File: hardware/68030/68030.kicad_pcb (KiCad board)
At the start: 2 copper layers, 99.1 x 99.1 mm, 20 parts, among them J1 nuMezzanine_4x34, U1 MC68030RC25B

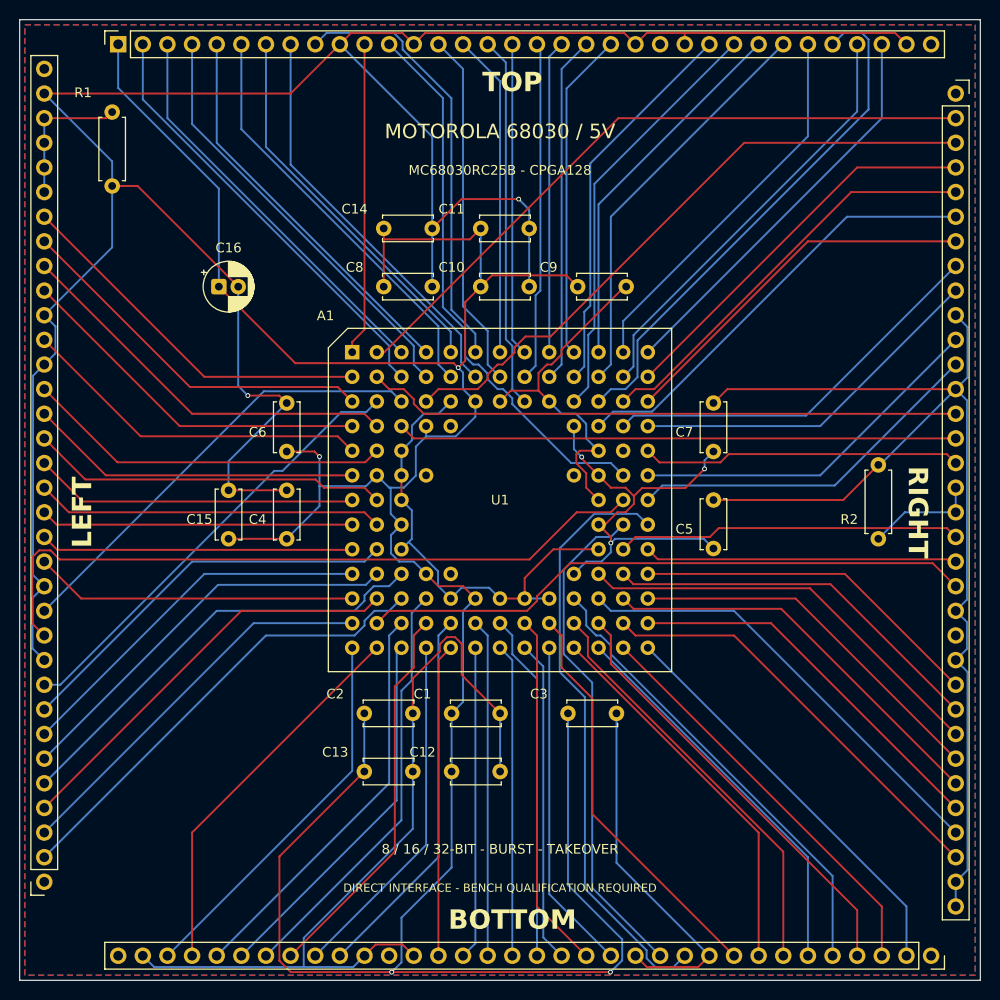
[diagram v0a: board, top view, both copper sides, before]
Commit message: Update mainboard to revision 2
Add an additional 8 bidirectional channels
Replace SPI PSRAM with hyperram
Remove LEDs
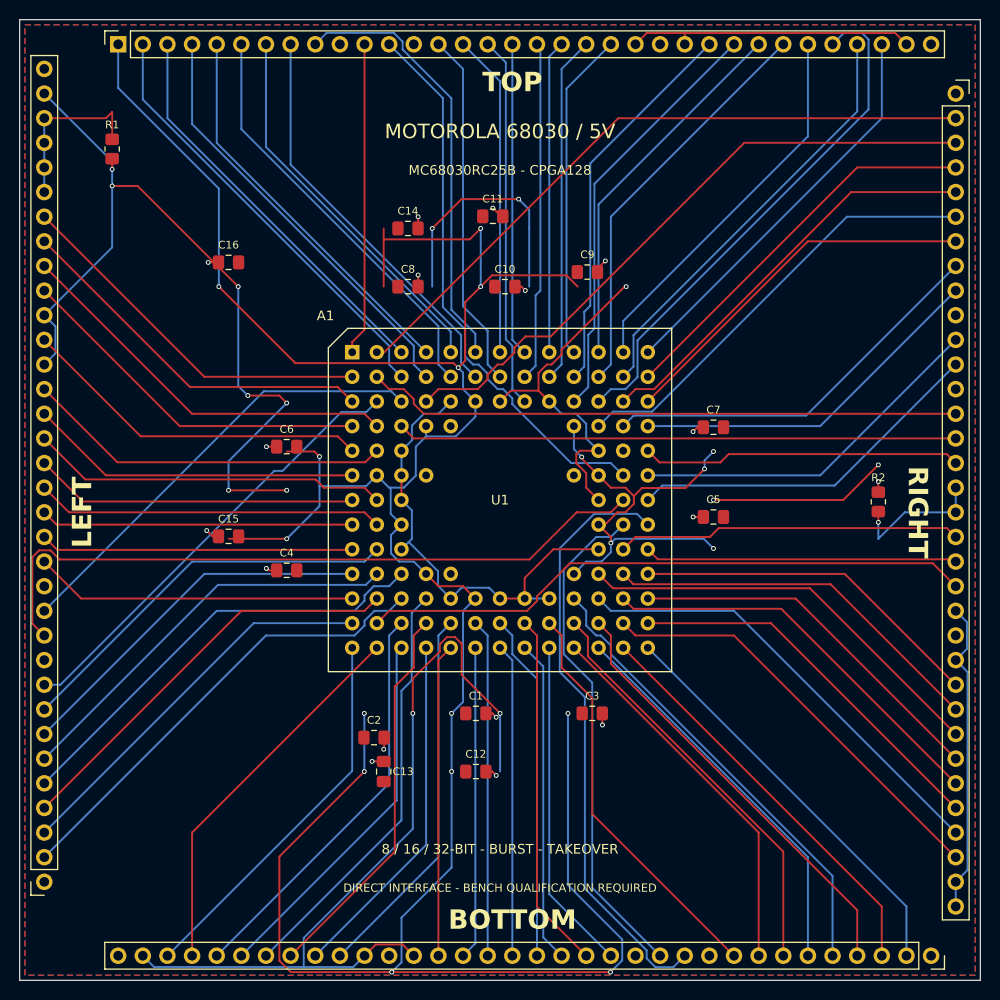
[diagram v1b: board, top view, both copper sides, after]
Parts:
- C1, C10, C11, C12, C13, C14, C15, C2, C3, C4, C5, C6, C7, C8, C9: footprint Capacitor_THT:C_Disc_D5.0mm_W2.5mm_P5.00mm -> Capacitor_SMD:C_0805_2012Metric_Pad1.18x1.45mm_HandSolder
- C16: footprint Capacitor_THT:CP_Radial_D5.0mm_P2.00mm -> Capacitor_SMD:C_0805_2012Metric_Pad1.18x1.45mm_HandSolder
- R1, R2: footprint Resistor_THT:R_Axial_DIN0207_L6.3mm_D2.5mm_P7.62mm_Horizontal -> Resistor_SMD:R_0805_2012Metric_Pad1.20x1.40mm_HandSolder
- moved R1 3.81 mm to (111.0, 59.8)
- moved R2 3.81 mm to (190.0, 96.2)
- moved C4 3.25 mm to (129.0, 103.2), turned to 180 degrees
- moved C5 3.25 mm to (173.0, 97.8), turned to 180 degrees
- moved C16 2.69 mm to (123.0, 71.5), turned to 180 degrees
- moved C2 2.69 mm to (138.0, 120.5)
- moved C1 2.50 mm to (148.5, 118.0)
- moved C10 2.50 mm to (151.5, 74.0)
- moved C12 2.50 mm to (148.5, 124.0)
- moved C14 2.50 mm to (141.5, 68.0)
- moved C3 2.50 mm to (160.5, 118.0)
- moved C7 2.50 mm to (173.0, 88.5), turned to 180 degrees
- moved C8 2.50 mm to (141.5, 74.0)
- moved C13 2.00 mm to (139.0, 124.0), turned to 90 degrees
- moved C9 1.80 mm to (160.0, 72.5)
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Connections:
- net /BX renamed /BX1
- net /BY renamed /BX2
- net /LX renamed /LX1
- net /LY renamed /LX2
- net /RX renamed /RX1
- net /RY renamed /RX2
- net /TX renamed /TX1
- net /TY renamed /TX2
- J1 pad 10: GND -> unconnected-(J1A-TX3-Pad10)
- J1 pad 102: unconnected-(J1E-NC-Pad102) -> GND
- J1 pad 112: GND -> unconnected-(J1B-LX3-Pad112)
- J1 pad 115: GND -> unconnected-(J1B-LX0-Pad115)
- J1 pad 13: GND -> unconnected-(J1A-TX0-Pad13)
- J1 pad 136: unconnected-(J1E-NC-Pad136) -> GND
- J1 pad 44: GND -> unconnected-(J1D-RX3-Pad44)
- J1 pad 47: GND -> unconnected-(J1D-RX0-Pad47)
- J1 pad 78: GND -> unconnected-(J1C-BX3-Pad78)
- J1 pad 81: GND -> unconnected-(J1C-BX0-Pad81)
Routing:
- net GND: track 591.7 -> 386.5 mm, vias 2 -> 31
- net /R1_UNUSED: track 11.7 -> 14.5 mm, vias 0 -> 1
- net /L0_UNUSED: track 14.9 -> 17.7 mm
- net /VCC_TL: vias 7 -> 18
